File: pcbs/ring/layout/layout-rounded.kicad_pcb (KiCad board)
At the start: 2 copper layers, 56 x 6.2 mm, 60 parts, among them J1 ?, Q1 CSD13380F3T, Q2 CSD13380F3T, U1 BQ27427YZFR, U2 BQ29700, U3 nRF52833-QDAA, U4 MAX30102EFD+T, U5 LSM6DSOX, U6 ?, U7 TMP117AIDRVR, U8 TPS7A2018PDQN, Y1 32MHz, Y2 32.768kHz

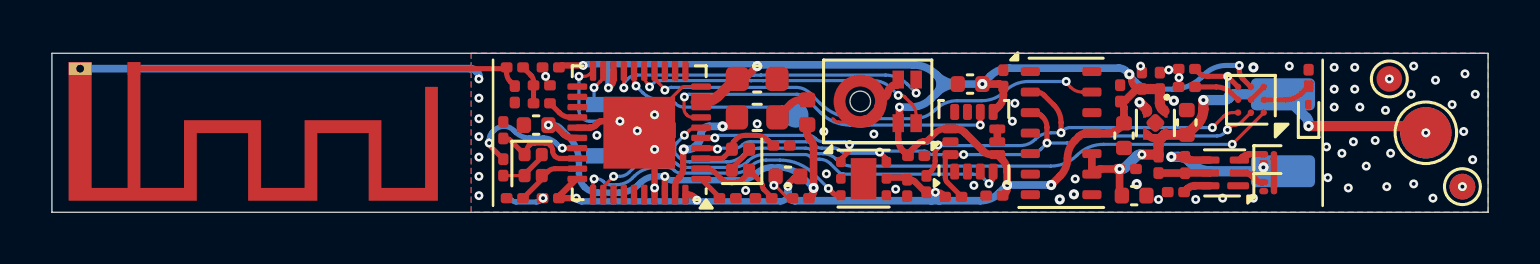
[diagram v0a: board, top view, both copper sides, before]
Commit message: added crystal mpns and updated caps
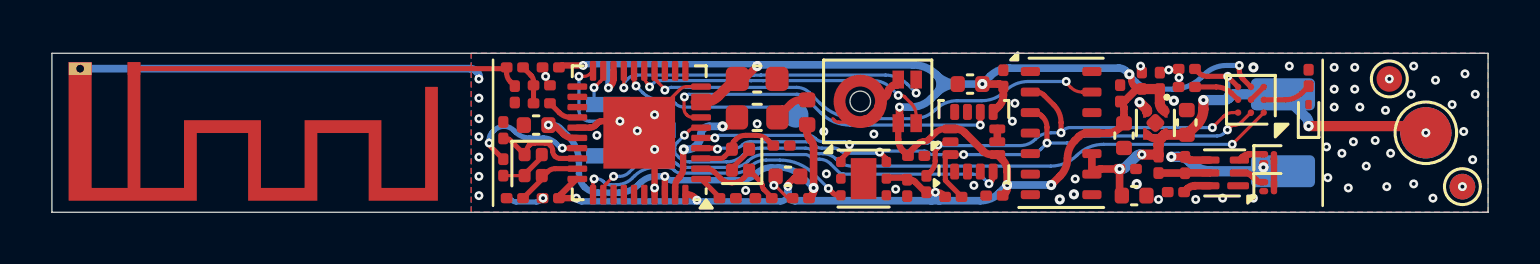
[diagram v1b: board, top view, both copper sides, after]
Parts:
- C4, C9: value 12pF -> 5pF
- Y1: value 32MHz -> 8J32076001
- Y2: value 32.768kHz -> 3110M4-32.768DTTLLLL

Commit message: rounded v2
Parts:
- removed D1: ESD9B5.0ST5G, D_SOD-923:D_SOD-923
- removed TP2, TP5: , TestPoint_Pad_D2.0mm:TestPoint_Pad_D2.0mm
- removed TP3, TP4, TP6: , TestPoint_Pad_D1.0mm:TestPoint_Pad_D1.0mm
- moved TP1 10.8 mm to (136.6, 81.2)
- moved C22 6.91 mm to (148.1, 85.2), turned to 90 degrees
- moved C26 5.87 mm to (147.9, 80.7), turned to 180 degrees
- moved C23 5.21 mm to (152.3, 85.2)
- moved R1 5.01 mm to (149.2, 82.8)
- moved C24 4.27 mm to (153.6, 85.5), turned to 0 degrees
- moved U5 4.18 mm to (150.2, 84.7), turned to 0 degrees
- moved U7 3.69 mm to (150.0, 81.2), turned to 180 degrees
- moved MK1 3.40 mm to (153.8, 82.2), turned to 90 degrees
- moved R2 2.86 mm to (150.7, 82.8), turned to 180 degrees
- moved C15 2.25 mm to (147.4, 83.4)
- moved C25 1.57 mm to (151.7, 82.5), turned to 90 degrees
- moved C6 0.42 mm to (147.2, 85.1), turned to 90 degrees
- moved C11 0.38 mm to (146.3, 83.8), turned to -90 degrees
- moved L2 0.22 mm to (147.7, 82.1)
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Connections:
- U3 pad 14: hbt_int -> mic_data
- U3 pad 15: mic_data -> mic_clk
- U3 pad 17: mic_clk -> tmp_int
- U3 pad 31: tmp_int -> imu_int2
- U3 pad 4: sda -> scl
- U3 pad 5: scl -> sda
- U3 pad 7: imu_int2 -> hbt_int
- U7 pad 4: GND -> VDD
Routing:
- net VDD: track 81.9 -> 74.0 mm
- net VBATT: track 21.1 -> 13.9 mm, vias 6 -> 2
- net GND: track 35.5 -> 28.9 mm, vias 68 -> 46
- net imu_int1: track 16.8 -> 11.6 mm
- net cpu.dec4_6: track 17.7 -> 14.9 mm
- net bat_low: track 25.7 -> 23.6 mm
- net rst: track 7.18 -> 5.52 mm
- net mic_clk: track 13.1 -> 14.7 mm
- net mic_data: track 12.1 -> 13.6 mm
- net scl: track 26.5 -> 27.7 mm
- net battery.bat_vss: track 6.21 -> 5.18 mm
- net tmp_int: track 11.1 -> 12.1 mm
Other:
- board size 56 x 6.2 mm -> 49.6 x 6.2 mm
